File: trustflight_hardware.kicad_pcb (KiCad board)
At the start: 2 copper layers, 27 x 27 mm, 68 parts, among them J1 Conn_01x02, J10 Dronecode_Telemetry, J2 Conn_01x02, J3 Conn_01x02, J4 Conn_01x02, J5 Conn_01x01, J6 Conn_01x02, J7 Conn_01x02, J8 Conn_01x03, J9 swd-4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

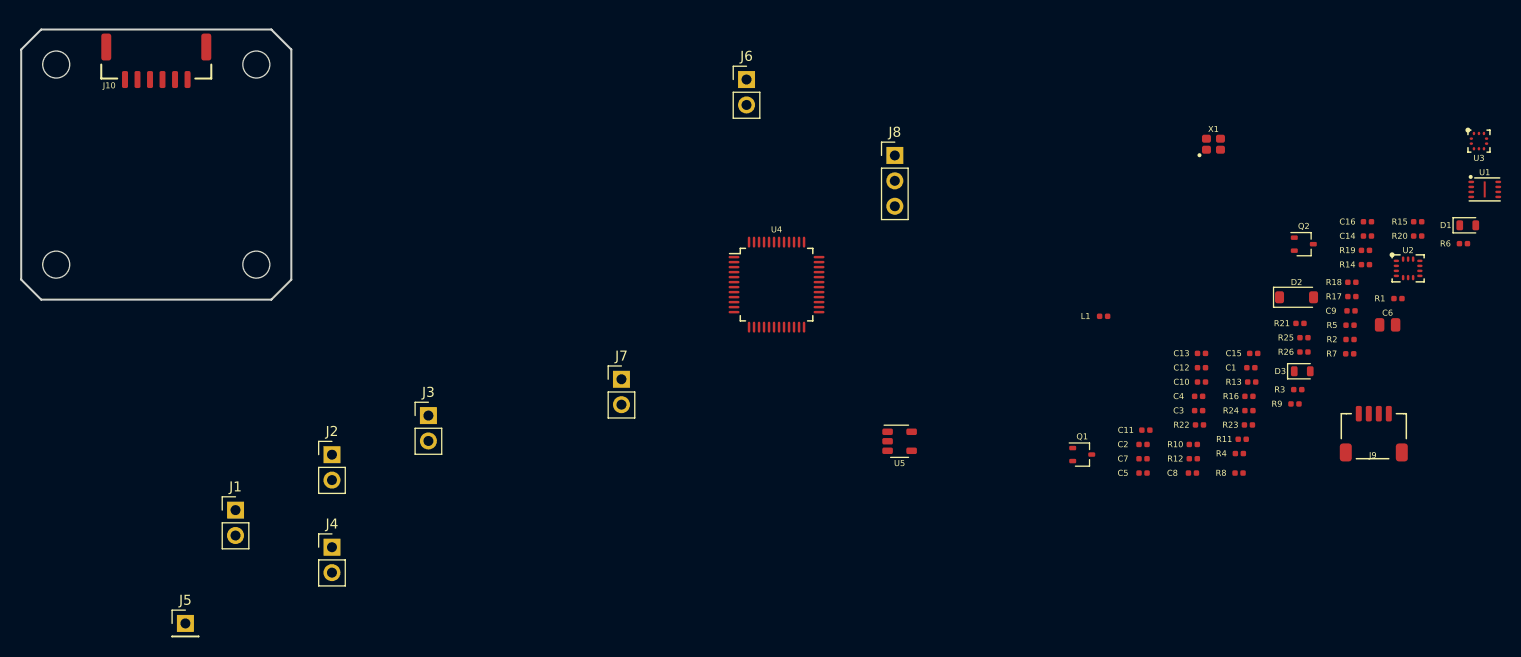
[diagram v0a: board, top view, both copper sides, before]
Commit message: All components on PCB, almost ready for routing
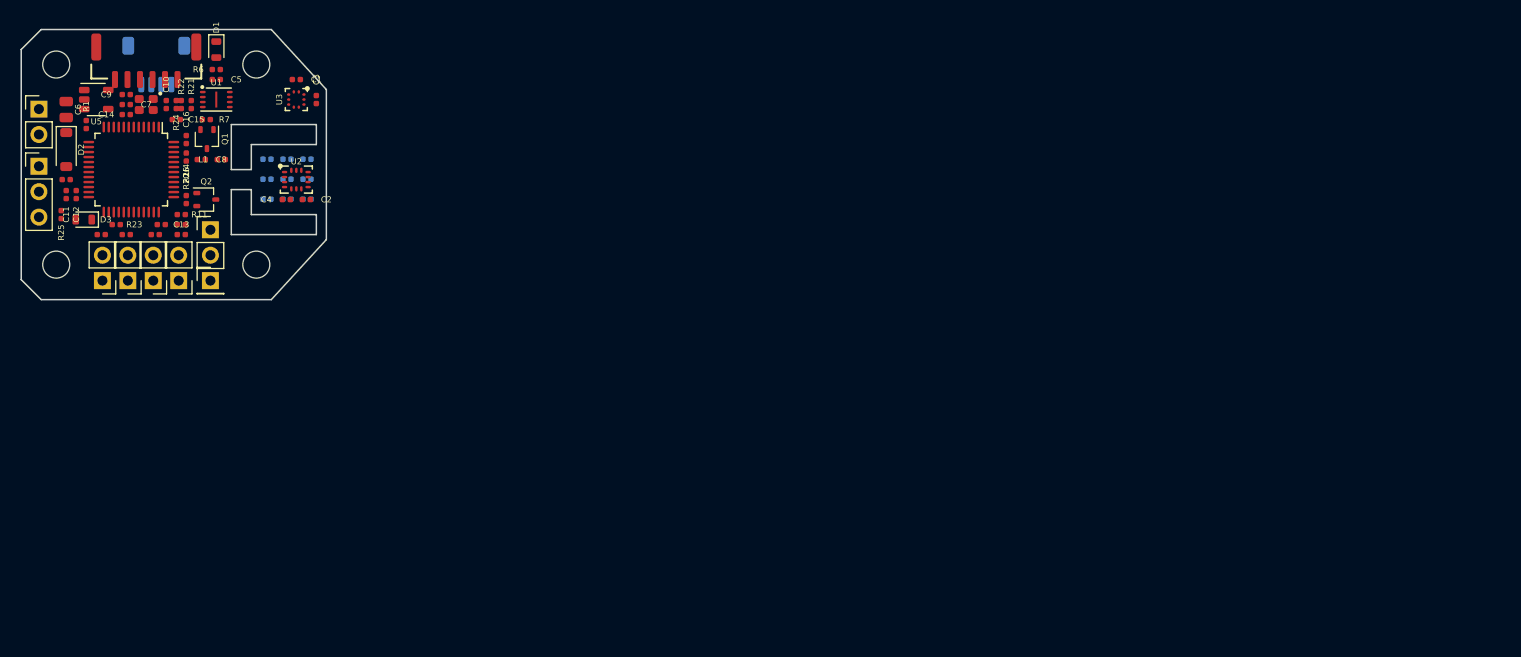
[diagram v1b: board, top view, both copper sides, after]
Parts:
- J9, R10, R13, R14, R15, R16, R17, R18, R8, R9: moved to B.Cu
- moved C6 133.8 mm to (131.0, 84.5), turned to 270 degrees
- moved R1 132.3 mm to (133.0, 86.0), turned to 270 degrees
- moved R19 130.1 mm to (131.0, 91.5)
- moved U1 127.1 mm to (146.0, 83.5)
- moved D1 126.3 mm to (146.0, 78.5), turned to 270 degrees
- moved J9 126.1 mm to (140.0, 82.0)
- moved R6 125.9 mm to (146.0, 80.5)
- moved R2 125.3 mm to (134.5, 97.0)
- moved R25 124.8 mm to (130.5, 95.0), turned to 90 degrees
- moved C14 124.7 mm to (137.0, 85.0)
- moved C9 124.3 mm to (137.0, 83.0)
- moved D2 123.9 mm to (131.0, 88.5), turned to 270 degrees
- moved R20 123.1 mm to (143.0, 93.5), turned to 270 degrees
- moved D3 122.7 mm to (132.8, 95.5), turned to 180 degrees
- moved C16 118.4 mm to (143.0, 87.5), turned to 270 degrees
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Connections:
- net Net-(D3-Pad1) renamed /LED
- net Net-(J1-Pad2) renamed /M1_P
- net Net-(J2-Pad2) renamed /M2_P
- net Net-(J3-Pad2) renamed /M3_P
- net Net-(J4-Pad2) renamed /M4_P
- net Net-(J7-Pad2) renamed /BUZZ_P
- net Net-(J8-Pad2) renamed /F.port_P
- net Net-(Q1-Pad3) renamed /V_HEAT
- J5 pad 1: /ESC_TLM -> /ESC_TLM_P
- R11 pad 1: /ESC_TLM -> /ESC_TLM_P
- R12 pad 1: /ESC_TLM -> /ESC_TLM_P
- R12 pad 2: Net-(R12-Pad2) -> /ESC_TLM
- U4 pad 22: Net-(R12-Pad2) -> /ESC_TLM
- U4 pad 42: Net-(U4-Pad42) -> /COM_TX
- U4 pad 43: Net-(U4-Pad43) -> /COM_RX
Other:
- board size 27 x 27 mm -> 30.5 x 27 mm

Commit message: Fixed VSYS
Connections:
- C6 pad 1: /VIN -> /VSYS
- D2 pad 1: /VIN -> /VSYS
- J8 pad 3: +5V -> /VSYS
- Q1 pad 2: +5V -> /VSYS
- Q2 pad 2: +5V -> /VSYS
- R20 pad 2: +5V -> /VSYS
- R25 pad 2: /VIN -> /VSYS
- R7 pad 2: +5V -> /VSYS
- U5 pad 1: /VIN -> /VSYS
- U5 pad 3: /VIN -> /VSYS

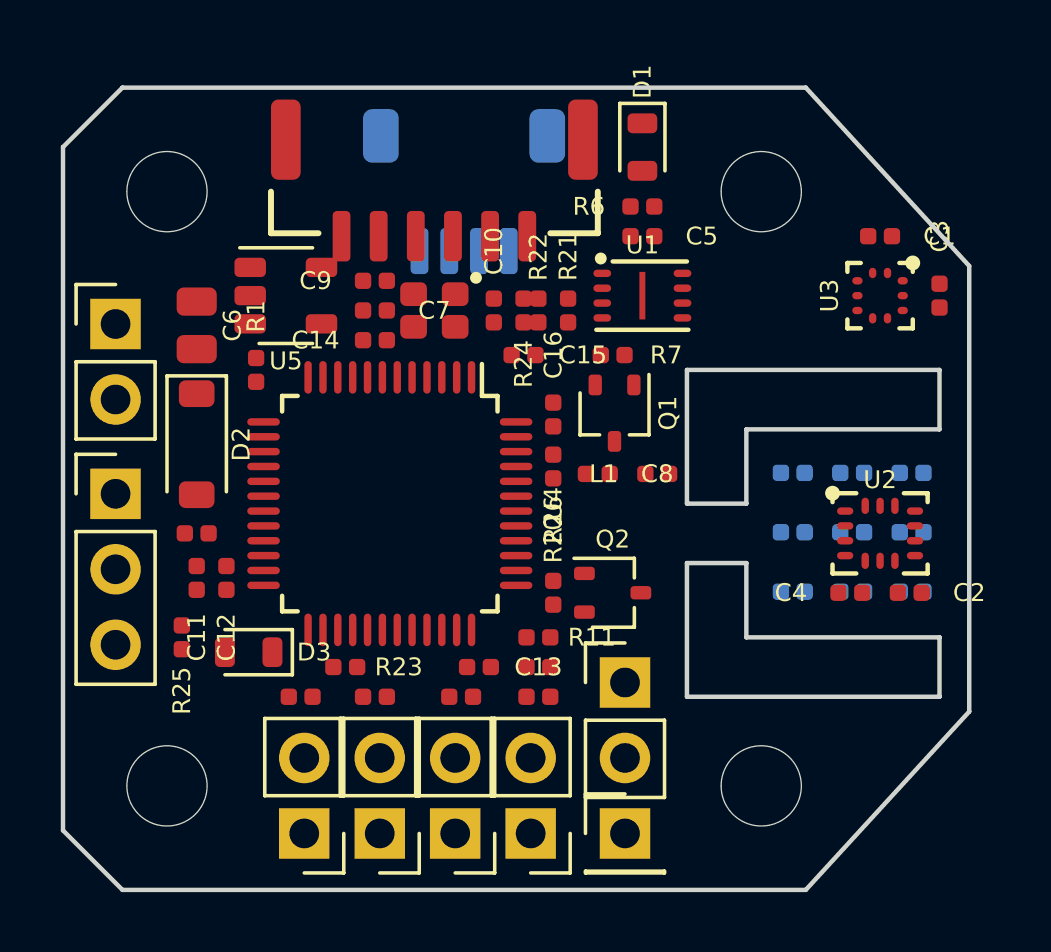
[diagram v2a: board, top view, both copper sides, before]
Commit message: Most of PCB routing is done
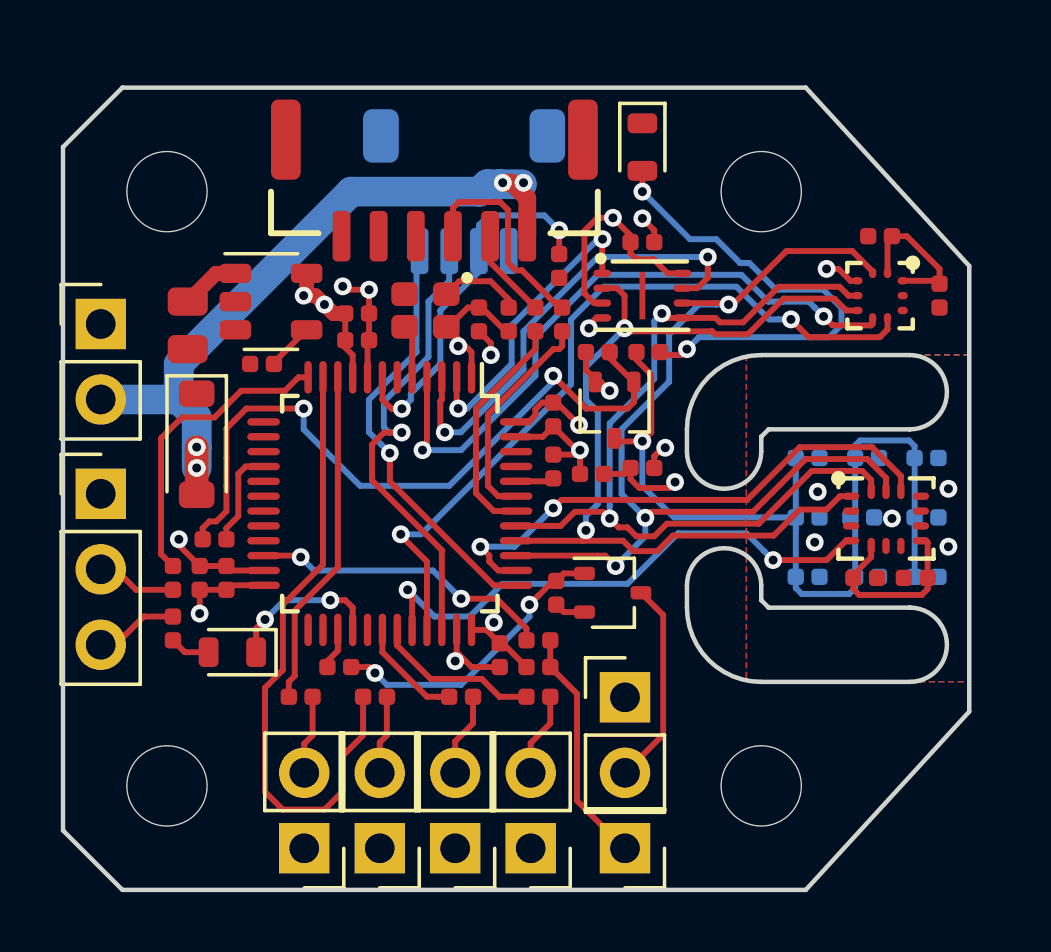
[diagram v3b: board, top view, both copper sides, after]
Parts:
- moved R1 5.87 mm to (131.6, 91.7), turned to 0 degrees
- moved R6 4.90 mm to (146.2, 85.4)
- moved C7 4.20 mm to (133.2, 85.8)
- moved C15 3.23 mm to (143.2, 82.5), turned to 90 degrees
- moved R19 1.70 mm to (130.2, 93.0), turned to 90 degrees
- moved C9 1.25 mm to (136.4, 84.1)
- moved R21 1.14 mm to (142.4, 84.3)
- moved R11 1.00 mm to (142.5, 96.0)
- moved R12 0.90 mm to (142.5, 95.1)
- moved R22 0.85 mm to (143.3, 84.3)
- moved C13 0.81 mm to (141.2, 95.6), turned to 270 degrees
- moved C4 0.71 mm to (153.5, 93.0)
- moved R13 0.71 mm to (155.6, 91.0)
- moved R14 0.71 mm to (151.6, 93.0)
- moved R15 0.71 mm to (155.6, 89.0)
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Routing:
- net /SCK: track 0.00 -> 32.4 mm, vias 0 -> 3
- net /MISO: track 0.00 -> 31.0 mm, vias 0 -> 2
- net /V_HEAT: track 0.00 -> 29.2 mm, vias 0 -> 1
- net /MOSI: track 0.00 -> 28.9 mm, vias 0 -> 2
- net +3V3: track 0.00 -> 26.6 mm, vias 0 -> 8
- net /BAR_INT: track 0.00 -> 25.9 mm, vias 0 -> 2
- net +5V: track 0.00 -> 23.9 mm, vias 0 -> 4
- net Net-(Q1-Pad1): track 0.00 -> 23.8 mm, vias 0 -> 2
- net /BAR_CS: track 0.00 -> 21.8 mm, vias 0 -> 2
- net /M2: track 0.00 -> 21.3 mm
- net /IMU_INT: track 0.00 -> 18.5 mm, vias 0 -> 2
- net GND: track 0.00 -> 18.2 mm, vias 0 -> 14
- net /IMU_CS: track 0.00 -> 18.1 mm, vias 0 -> 2
- net Net-(D1-Pad2): track 0.00 -> 16.1 mm, vias 0 -> 2
- net /SWDIO: track 0.00 -> 15.9 mm, vias 0 -> 1
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- added copper zone on B.Cu, net GND
- added copper zone on F.Cu, net GND
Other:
- outline, holes or cut-outs redrawn

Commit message: No DRC errors, all routed
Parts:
- Q1, Q2: value BC807W -> DMG1013UW
- R1, R23: value 1k -> 180
- moved C15 0.20 mm to (143.4, 82.5)
- moved C6 0.20 mm to (130.5, 84.5)
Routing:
- net /VSYS: track 7.11 -> 80.7 mm, vias 1 -> 4
- net VAA: track 14.4 -> 40.1 mm, vias 1 -> 3
- net GND: track 18.2 -> 31.8 mm, vias 14 -> 60
- net +3V3: track 26.6 -> 27.5 mm
- added copper zone on In1.Cu, net +3V3
- added copper zone on In1.Cu, net GND
- added copper zone on In2.Cu, net GND
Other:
- copper layers 2 -> 4

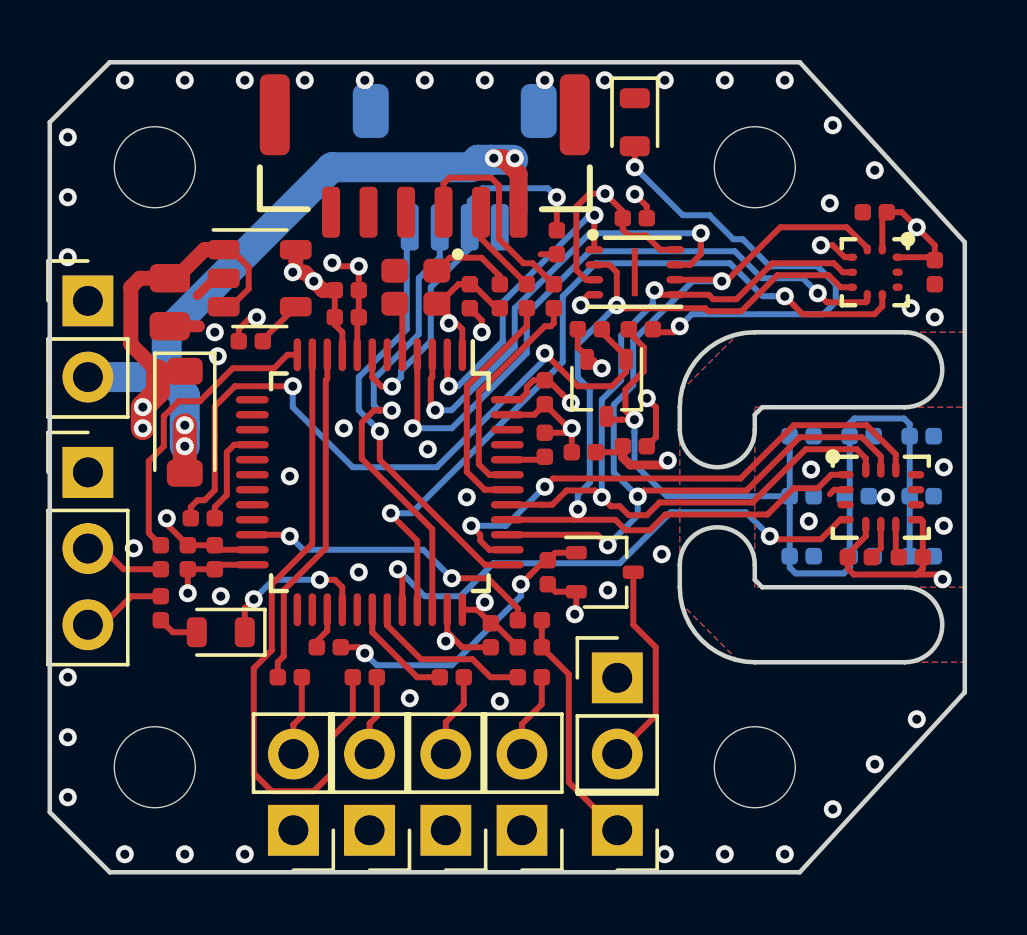
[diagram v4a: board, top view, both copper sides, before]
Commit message: Added silkscreen and some finishing touches
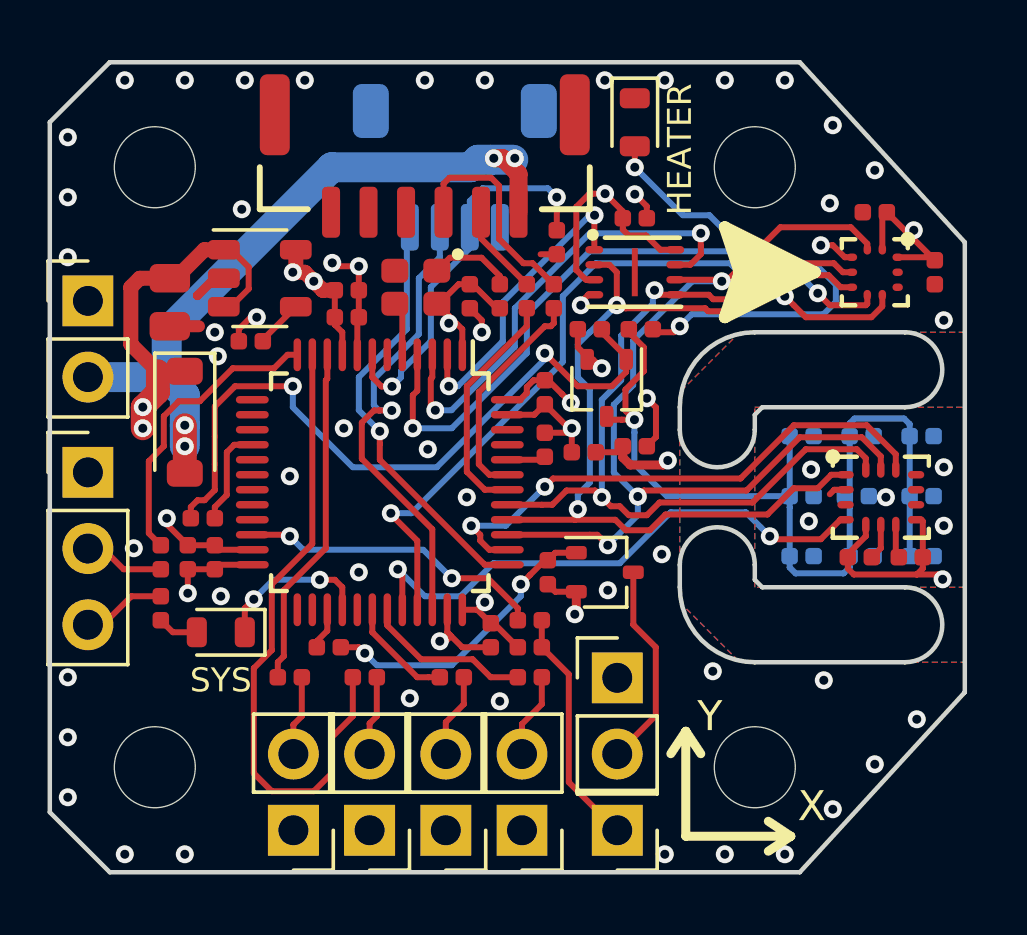
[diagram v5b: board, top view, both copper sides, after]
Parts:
- added LOGO1: Logo_Open_Hardware_Small, Symbol:OSHW-Symbol_6.7x6mm_SilkScreen, B.Cu at (140.3, 90.2)
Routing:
- net GND: vias 60 -> 59
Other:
- board text added: "+5V"
- board text added: "B"
- board text added: "CERN-OHL"
- board text added: "CLK"
- board text added: "Emil Fresk 2018"
- board text added: "GND"
- board text added: "HEATER"
- board text added: "M1"
- board text added: "M2"
- board text added: "M3"
- board text added: "M4"
- board text added: "RC"
- board text added: "RST"
- board text added: "Rev. A"
- board text added: "SIO"
- board text added: "SYS"
- board text added: "T"
- board text added: "TrustFlight"
- board text added: "V"
- board text added: "X"
- board text added: "Y"

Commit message: More additions
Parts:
- U4: value stm32f302x -> STM32F302CBT6
- U5: value MIC5205-3.3 -> MIC5318-3.3YD5
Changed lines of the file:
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@@
       (plotinvisibletext false)
       (padsonsilk false)
-      (subtractmaskfromsilk false)
+      (subtractmaskfromsilk true)
       (outputformat 1)
       (mirror false)
-      (drillshape 1)
+      (drillshape 0)
       (scaleselection 1)
-      (outputdirectory ""))
+      (outputdirectory gerbers/))
   )
   (net 0 "")
@@
       (effects (font (size 0.6 0.6) (thickness 0.13)))
     )
-    (fp_text value MIC5205-3.3 (at 1.3 0 90) (layer F.Fab) hide
+    (fp_text value MIC5318-3.3YD5 (at 1.3 0 90) (layer F.Fab) hide
       (effects (font (size 0.3 0.3) (thickness 0.05)))
     )
@@
       (effects (font (size 0.6 0.6) (thickness 0.13)))
     )
-    (fp_text value stm32f302x (at 0 3.1 270) (layer F.Fab) hide
+    (fp_text value STM32F302CBT6 (at 0 3.1 270) (layer F.Fab) hide
       (effects (font (size 0.4 0.4) (thickness 0.05)))
     )

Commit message: Updated values, shrunk copper planes under IMU
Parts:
- D1: value LED -> LED_RED
- D3: value LED -> LED_BLUE
- R1, R23: value 180 -> 100
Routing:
- net GND: track 31.8 -> 32.3 mm
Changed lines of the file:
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@@
   (general
     (thickness 1.6)
-    (drawings 64)
-    (tracks 742)
+    (drawings 65)
+    (tracks 741)
     (zones 0)
     (modules 69)
@@
       (effects (font (size 0.6 0.6) (thickness 0.13)))
     )
-    (fp_text value LED (at 0 0.7 270) (layer F.Fab)
+    (fp_text value LED_RED (at 0 0.7 270) (layer F.Fab)
       (effects (font (size 0.3 0.3) (thickness 0.05)))
     )
@@
       (effects (font (size 0.6 0.6) (thickness 0.13)))
     )
-    (fp_text value LED (at 0 -0.8 180) (layer F.Fab)
+    (fp_text value LED_BLUE (at 0 -0.8 180) (layer F.Fab)
       (effects (font (size 0.3 0.3) (thickness 0.05)))
     )
@@
       (effects (font (size 0.6 0.6) (thickness 0.13)))
     )
-    (fp_text value 180 (at 0 -0.6) (layer F.Fab)
+    (fp_text value 100 (at 0 -0.6) (layer F.Fab)
       (effects (font (size 0.3 0.3) (thickness 0.05)))
     )
@@
       (effects (font (size 0.6 0.6) (thickness 0.13)))
     )
-    (fp_text value 180 (at 1.3 0 180) (layer F.Fab)
+    (fp_text value 100 (at 1.3 0 180) (layer F.Fab)
       (effects (font (size 0.3 0.3) (thickness 0.05)))
     )
@@
     )
   )
+  (gr_circle (center 147.7 102.3) (end 148 102.3) (layer F.SilkS) (width 0.4))
   (gr_text RC (at 129.8 96.1) (layer B.SilkS)
     (effects (font (size 0.8 0.8) (thickness 0.2)) (justify mirror))
@@
   (via (at 154 99.9) (size 0.6) (drill 0.3) (layers F.Cu B.Cu) (net 4))
   (via (at 155.4 98.4) (size 0.6) (drill 0.3) (layers F.Cu B.Cu) (net 4))
-  (segment (start 151.875728 90.075728) (end 151.224272 90.075728) (width 0.3) (layer In2.Cu) (net 4))
-  (segment (start 151.224272 90.075728) (end 150.3 91) (width 0.3) (layer In2.Cu) (net 4))
-  (segment (start 150.3 91) (end 147.1 91) (width 0.3) (layer In2.Cu) (net 4))
-  (segment (start 146.9 91.2) (end 146.9 92.9) (width 0.3) (layer In2.Cu) (net 4))
-  (segment (start 147.1 91) (end 146.9 91.2) (width 0.3) (layer In2.Cu) (net 4))
   (segment (start 154.2 92.7) (end 153.9 93) (width 0.2) (layer F.Cu) (net 4))
   (segment (start 154.2 91.925) (end 154.2 92.7) (width 0.2) (layer F.Cu) (net 4))
@@
   (via (at 152.3 97.1) (size 0.6) (drill 0.3) (layers F.Cu B.Cu) (net 4))
   (via (at 148.6 96.8) (size 0.6) (drill 0.3) (layers F.Cu B.Cu) (net 4))
+  (segment (start 146.9 91.2) (end 146.9 92.9) (width 0.3) (layer In2.Cu) (net 4))
+  (segment (start 147.1 91) (end 146.9 91.2) (width 0.3) (layer In2.Cu) (net 4))
+  (segment (start 151.875728 90.075728) (end 151.875728 91) (width 0.3) (layer In2.Cu) (net 4))
+  (segment (start 151.875728 91) (end 147.1 91) (width 0.3) (layer In2.Cu) (net 4))
   (via (at 144.9 91) (size 0.6) (drill 0.3) (layers F.Cu B.Cu) (net 5))
   (segment (start 142.9 91.25) (end 141.75 91.25) (width 0.2) (layer F.Cu) (net 5))
@@
     (polygon
       (pts
-        (xy 150 88) (xy 157 88) (xy 157 94) (xy 150 94)
+        (xy 151.5 88) (xy 157 88) (xy 157 94) (xy 151.5 94)
       )
     )
@@
     (polygon
       (pts
-        (xy 150 88) (xy 157 88) (xy 157 94) (xy 150 94)
+        (xy 151.5 88) (xy 157 88) (xy 157 94) (xy 151.5 94)
       )
     )
@@
     (polygon
       (pts
-        (xy 150 88) (xy 157 88) (xy 157 94) (xy 150 94)
+        (xy 151.5 88) (xy 157 88) (xy 157 94) (xy 151.5 94)
       )
     )
@@
     (polygon
       (pts
-        (xy 150 88) (xy 157 88) (xy 157 94) (xy 150 94)
+        (xy 151.5 88) (xy 157 88) (xy 157 94) (xy 151.5 94)
       )
     )
